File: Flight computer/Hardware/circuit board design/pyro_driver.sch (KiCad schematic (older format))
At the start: 10 parts, among them J4 Conn_01x06_Female, U6 Si7232DN

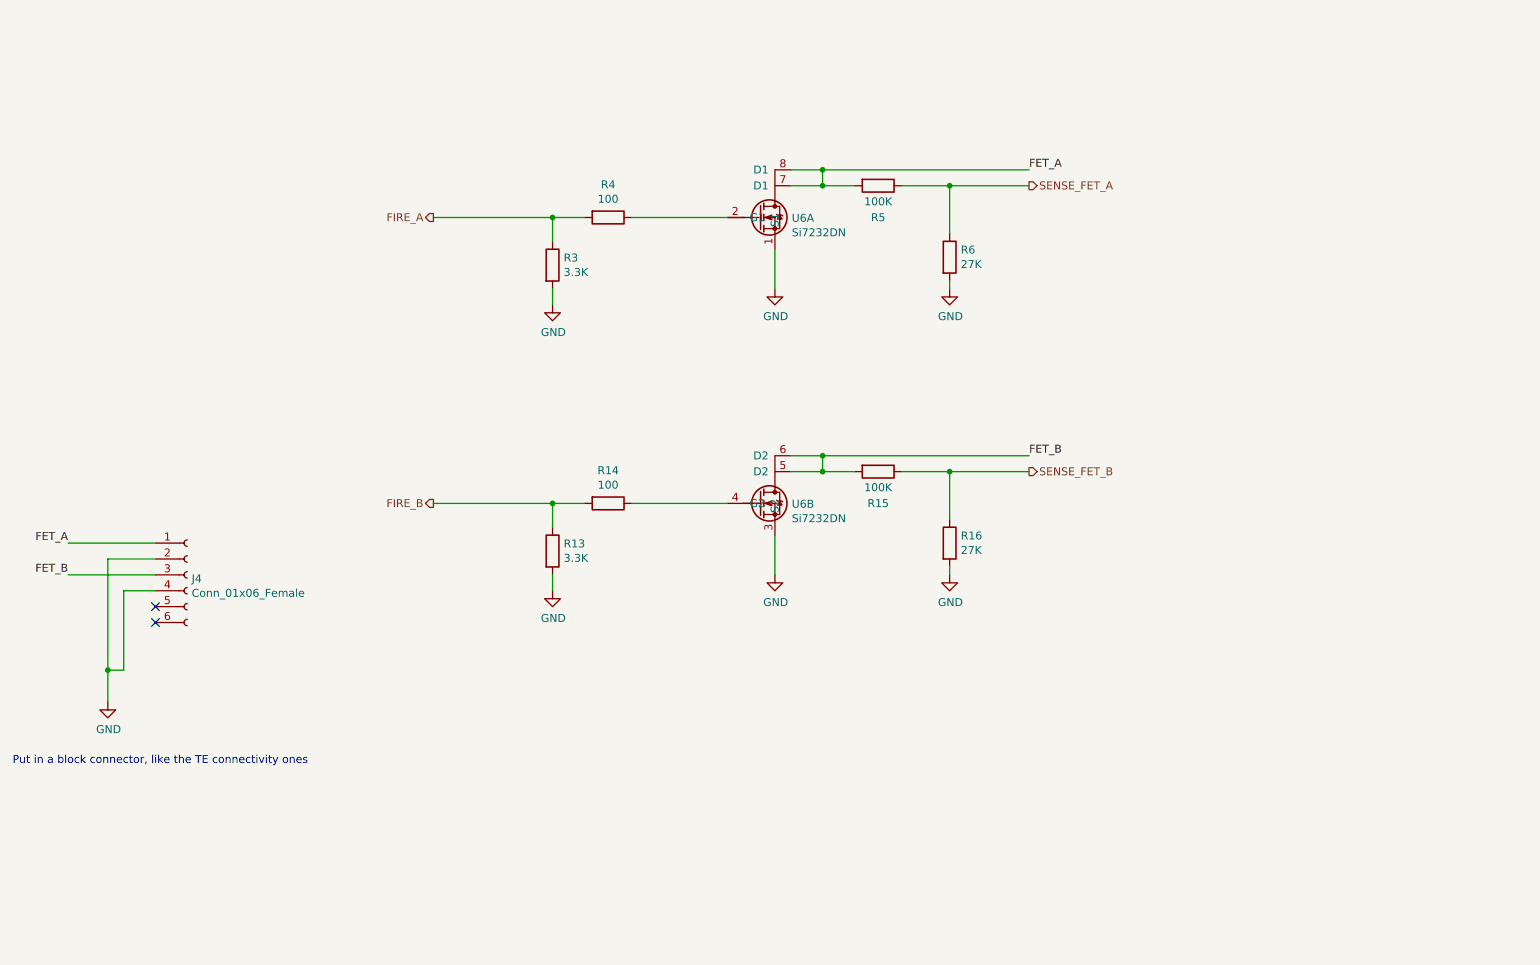
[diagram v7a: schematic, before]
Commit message: connected 4 channels of pyro drivers
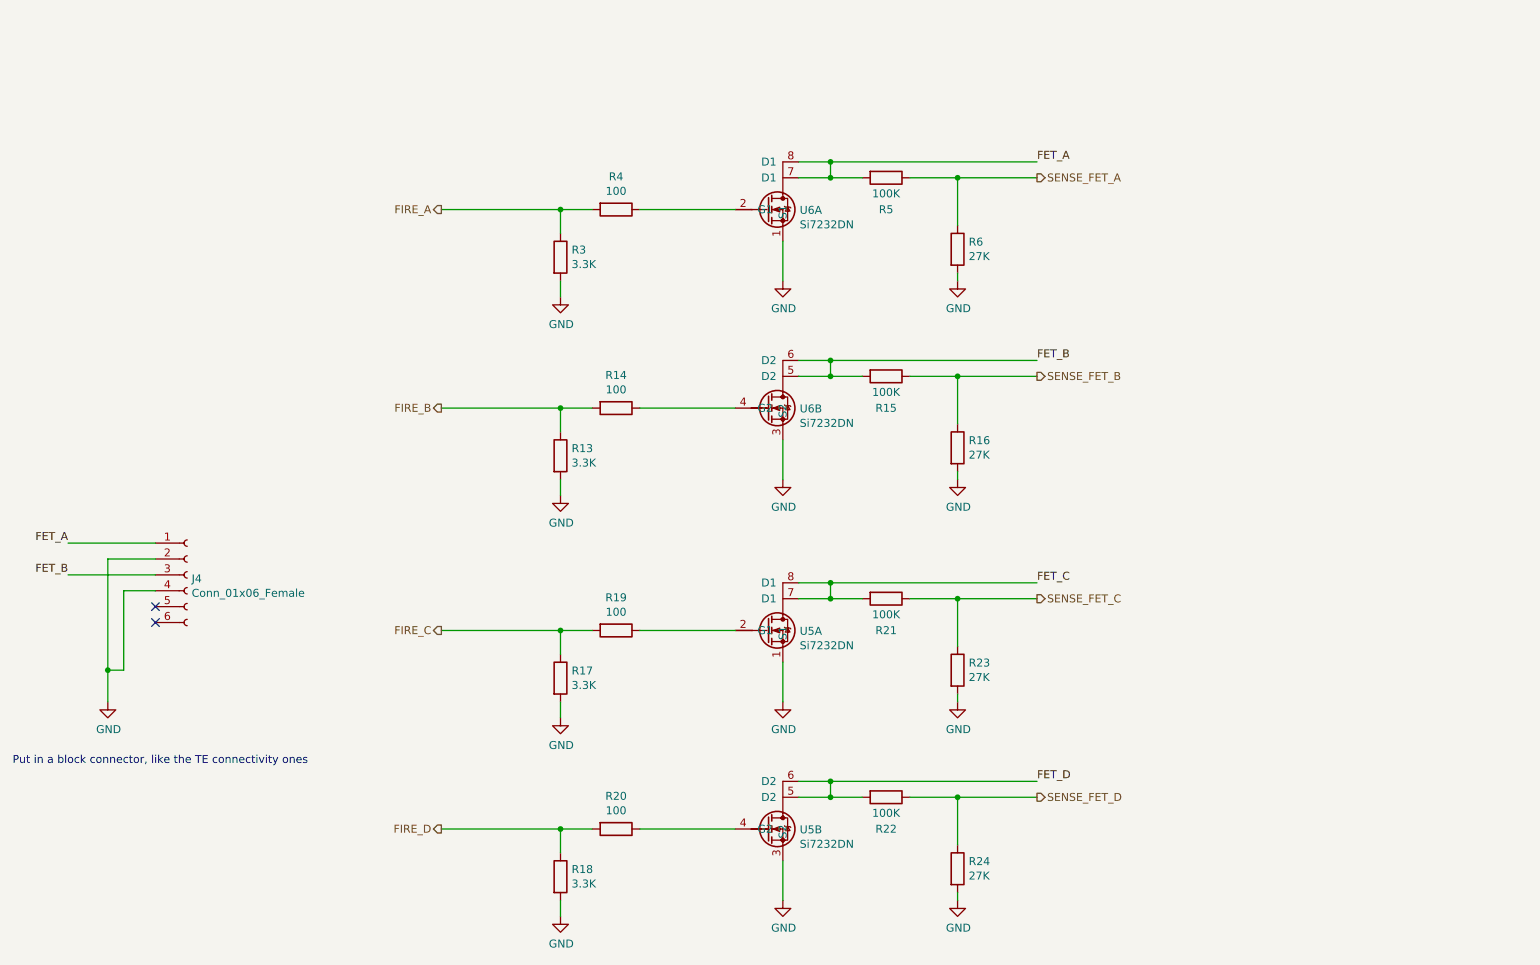
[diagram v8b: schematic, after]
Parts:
- added R17, R18: 3.3K, Resistor_SMD:R_0603_1608Metric, symbol Device:R
- added R19, R20: 100, Resistor_SMD:R_0603_1608Metric, symbol Device:R
- added R21, R22: 100K, Resistor_SMD:R_0603_1608Metric, symbol Device:R
- added R23, R24: 27K, Resistor_SMD:R_0603_1608Metric, symbol Device:R
- added U5: Si7232DN, Package_SO:Vishay_PowerPAK_1212-8_Dual, symbol circuit-board-design-rescue:Si7232DN-Driver_FET
- J4: footprint (none) -> TerminalBlock_TE-Connectivity:TerminalBlock_TE_282834-6_1x06_P2.54mm_Horizontal
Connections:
- net GND: now also R17.2, R18.2, R23.2, R24.2, U5.1 (S1), U5.3 (S2)
- new net: R19.1, U5.2 (G1)
- new net: R20.1, U5.4 (G2)
- new net FET_C: R21.2, U5.7 (D1), U5.8 (D1)
- new net FET_D: R22.2, U5.5 (D2), U5.6 (D2)
- new net FIRE_C: R17.1, R19.2
- new net FIRE_D: R18.1, R20.2
- new net SENSE_FET_C: R21.1, R23.1
- new net SENSE_FET_D: R22.1, R24.1
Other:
- moved on the sheet: R13, R14, R15, R16, R3, R4, R5, R6, U6A, U6B
